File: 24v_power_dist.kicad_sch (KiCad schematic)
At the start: 6 parts, among them J1 XT90PW-M

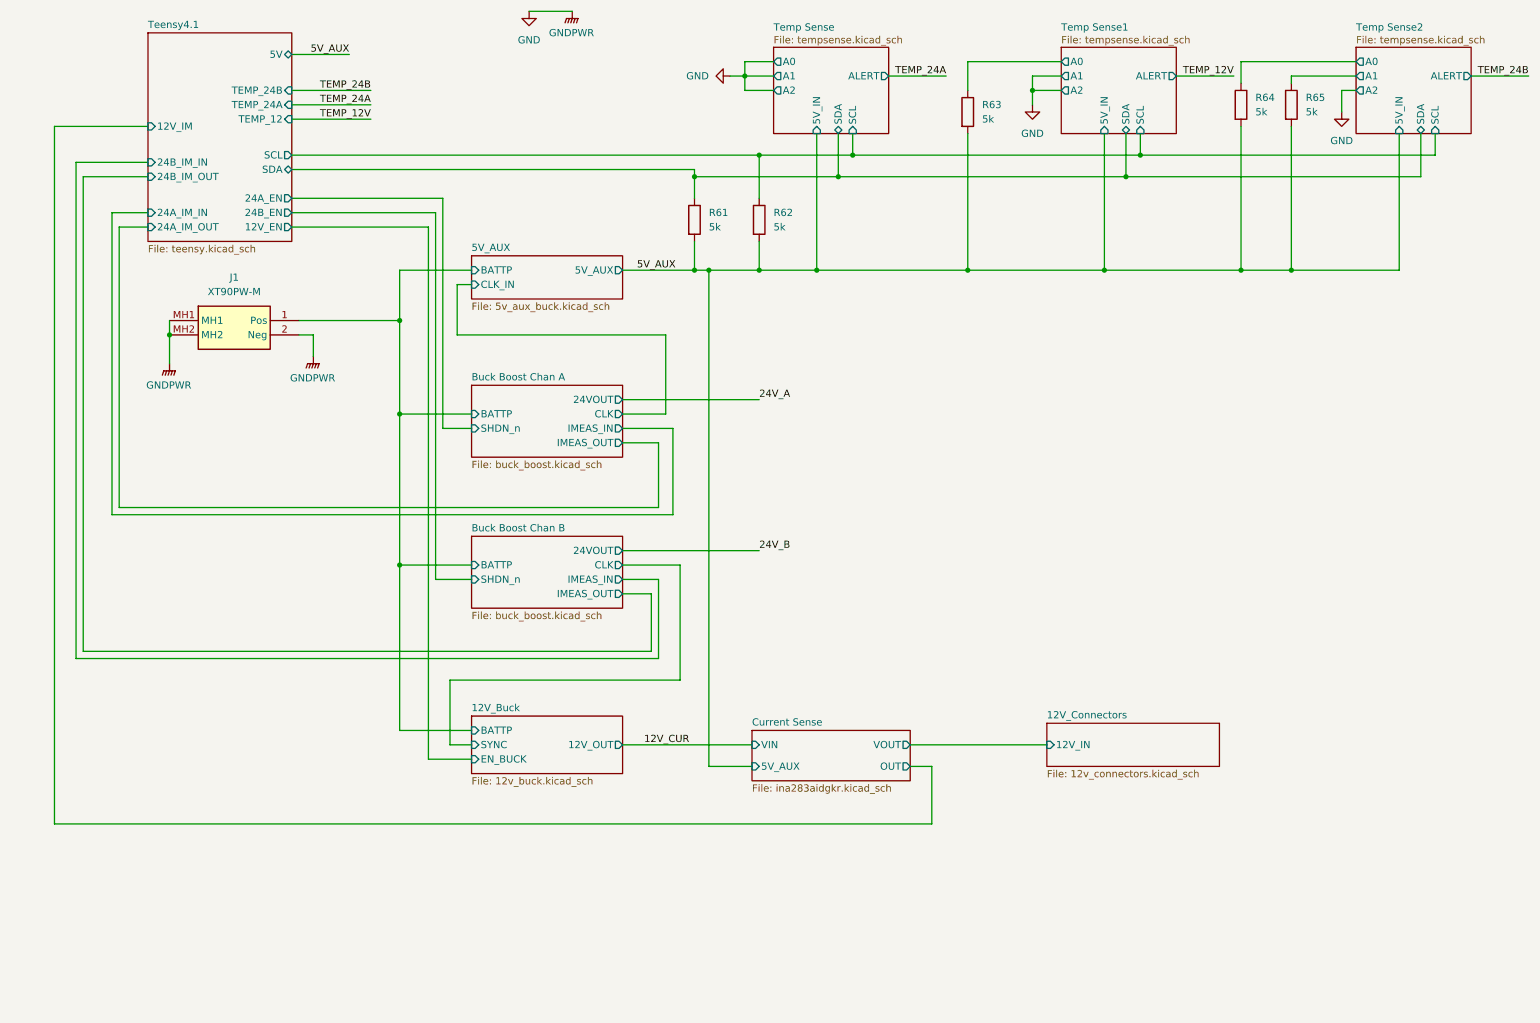
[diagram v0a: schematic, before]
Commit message: fixed 5 buck aux
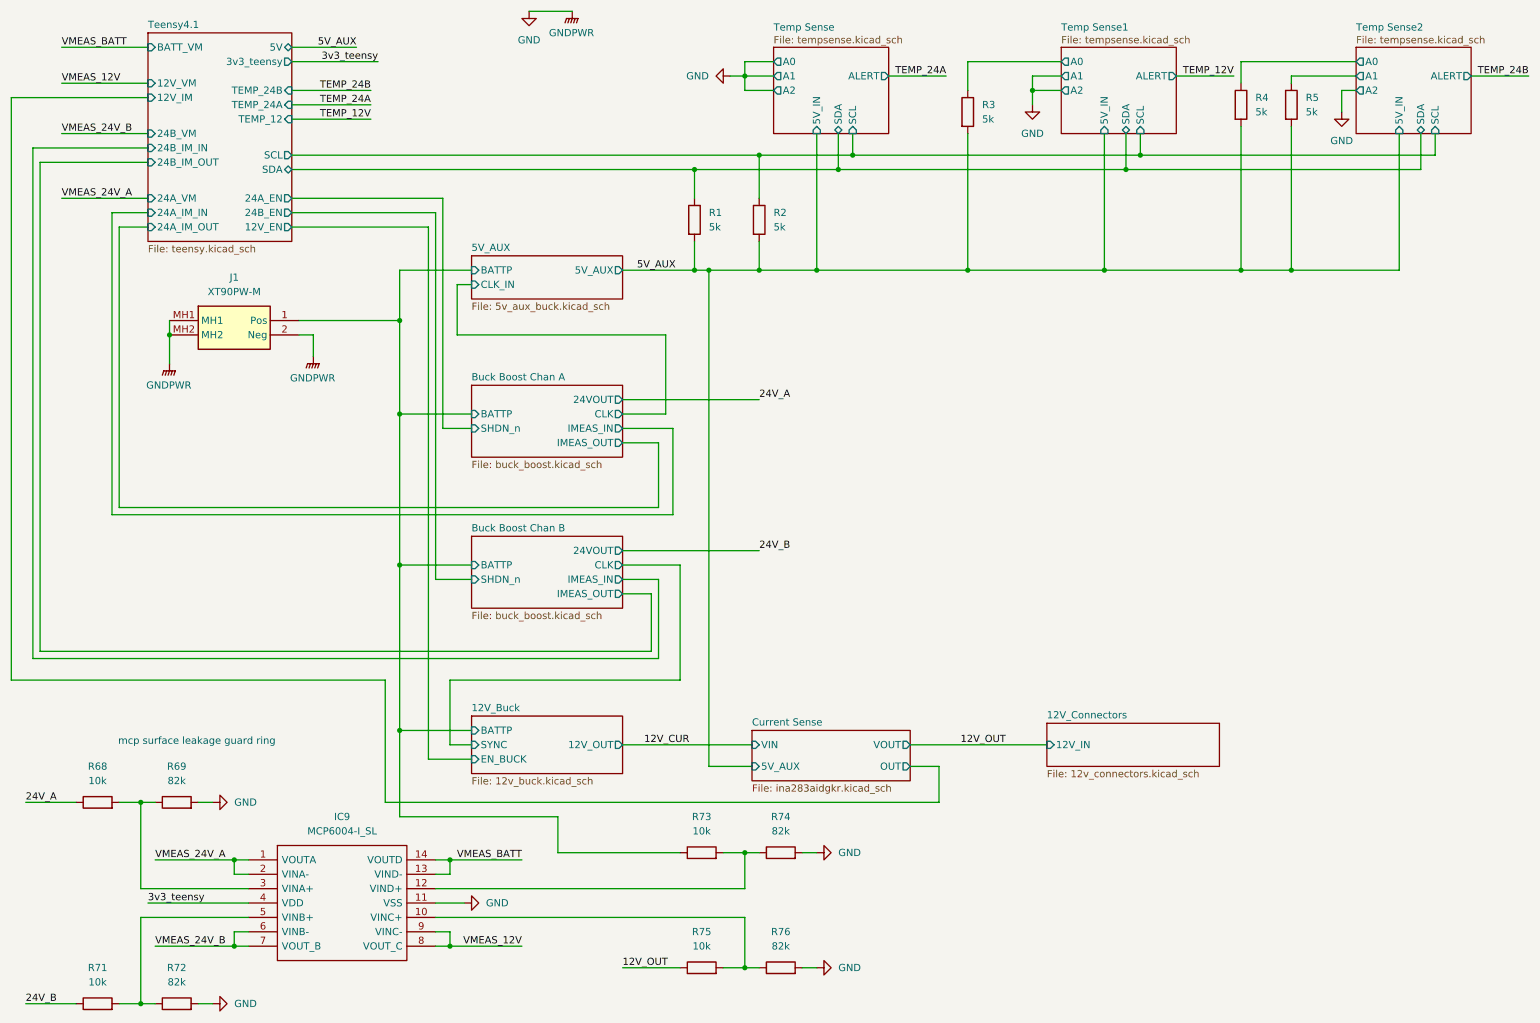
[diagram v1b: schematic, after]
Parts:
- added IC9: MCP6004-I_SL, SOIC127P600X175-14N, symbol power_dist:MCP6004-I_SL
- added R68, R71, R73, R75: 10k, symbol Device:R
- added R69, R72, R74, R76: 82k, symbol Device:R
- R1: renamed from R61; footprint (none) -> Resistor_SMD:R_0603_1608Metric
- R2: renamed from R62; footprint (none) -> Resistor_SMD:R_0603_1608Metric
- R3: renamed from R63; footprint (none) -> Resistor_SMD:R_0603_1608Metric
- R4: renamed from R64; footprint (none) -> Resistor_SMD:R_0603_1608Metric
- R5: renamed from R65; footprint (none) -> Resistor_SMD:R_0603_1608Metric
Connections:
- net 12V_Buck/BATTP: now also R73.1
- net 24V_A: now also R68.1
- net 24V_B: now also R71.1
- net GND: now also IC9.11 (VSS), R69.2, R72.2, R74.2, R76.2
- new net: IC9.3 (VINA+), R68.2, R69.1
- new net: IC9.12 (VIND+), R73.2, R74.1
- new net: IC9.10 (VINC+), R75.2, R76.1
- new net: IC9.5 (VINB+), R71.2, R72.1
- new net 12V_OUT: R75.1
- new net 3v3_teensy: IC9.4 (VDD)
- new net VMEAS_12V: IC9.8 (VOUT_C), IC9.9 (VINC-)
- new net VMEAS_24V_A: IC9.1 (VOUTA), IC9.2 (VINA-)
- new net VMEAS_24V_B: IC9.6 (VINB-), IC9.7 (VOUT_B)
- new net VMEAS_BATT: IC9.13 (VIND-), IC9.14 (VOUTD)
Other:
- sheet Teensy4.1 ports: added 12V_VM, 24A_VM, 24B_VM, 3v3_teensy, BATT_VM; removed none
- note added: "mcp surface leakage guard ring"

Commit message: assigned footprints
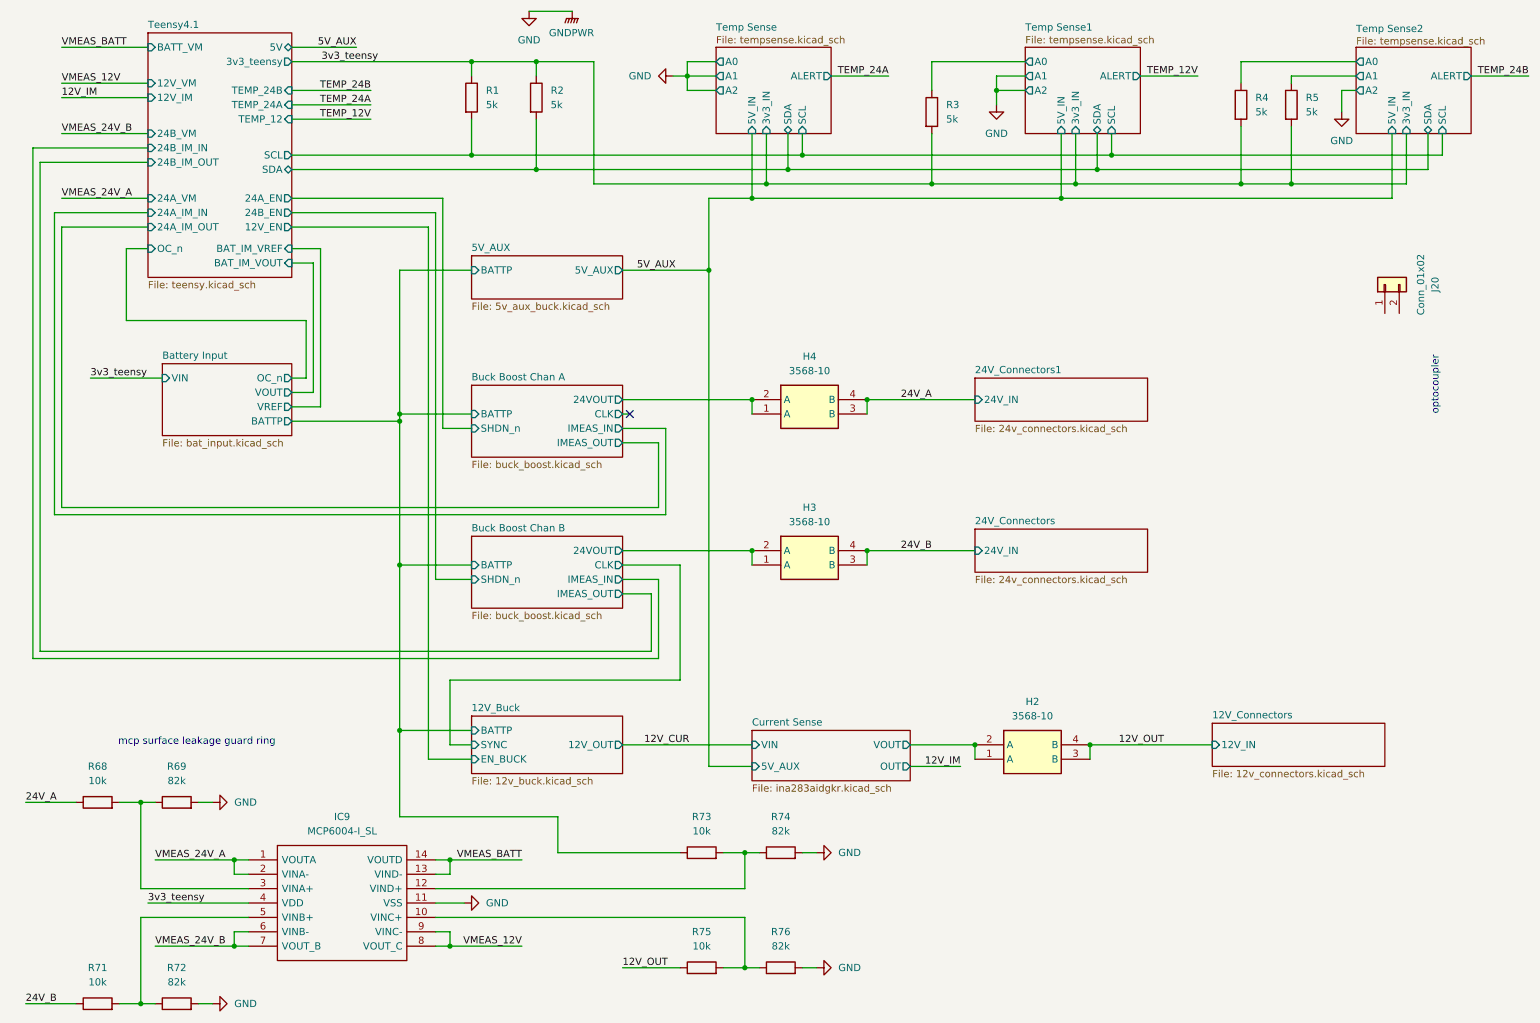
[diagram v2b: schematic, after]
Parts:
- removed J1: XT90PW-M, power_dist:XT90PWM, symbol power_dist:XT90PW-M
- added H2, H3, H4: 3568-10, power_dist:356810, symbol power_dist:3568-10
- added J20: Conn_01x02, Connector_JST:JST_PH_B2B-PH-K_1x02_P2.00mm_Vertical, symbol Connector_Generic:Conn_01x02
- IC9: footprint SOIC127P600X175-14N -> power_dist:MCP6004
- R68, R69, R71, R72, R73, R74, R75, R76: footprint (none) -> Resistor_SMD:R_0603_1608Metric
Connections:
- net 12V_OUT: now also H2.3 (B), H2.4 (B)
- net 24V_A: now also H4.3 (B), H4.4 (B)
- net 24V_B: now also H3.3 (B), H3.4 (B)
- net 3v3_teensy: now also R1.1, R2.1, R3.2, R4.2, R5.2
- net 5V_AUX: no longer R1.2, R2.2, R3.2, R4.2, R5.2
- net Teensy4.1/SCL: now also R1.2; no longer R2.1
- net Teensy4.1/SDA: now also R2.2; no longer R1.1
- new net Buck Boost Chan A/24VOUT: H4.1 (A), H4.2 (A)
- new net Buck Boost Chan B/24VOUT: H3.1 (A), H3.2 (A)
- new net Current Sense/VOUT: H2.1 (A), H2.2 (A)
- no-connect marks 0 -> 1
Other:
- added sheet 24V_Connectors (24v_connectors.kicad_sch)
- added sheet 24V_Connectors1 (24v_connectors.kicad_sch)
- added sheet Battery Input (bat_input.kicad_sch)
- sheet 5V_AUX ports: added none; removed CLK_IN
- sheet Teensy4.1 ports: added BAT_IM_VOUT, BAT_IM_VREF, OC_n; removed none
- sheet Temp Sense ports: added 3v3_IN; removed none
- sheet Temp Sense1 ports: added 3v3_IN; removed none
- sheet Temp Sense2 ports: added 3v3_IN; removed none
- note added: "optocoupler"
- moved on the sheet: R3
